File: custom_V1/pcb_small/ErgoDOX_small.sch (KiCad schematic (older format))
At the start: 61 parts, among them J1 Input, J10 Conn_01x01, J11 Conn_01x01, J12 Conn_01x01, J13 Conn_01x01, J14 Conn_01x01, J15 Conn_01x01, J16 Conn_01x01, J17 Conn_01x01, J18 Conn_01x01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

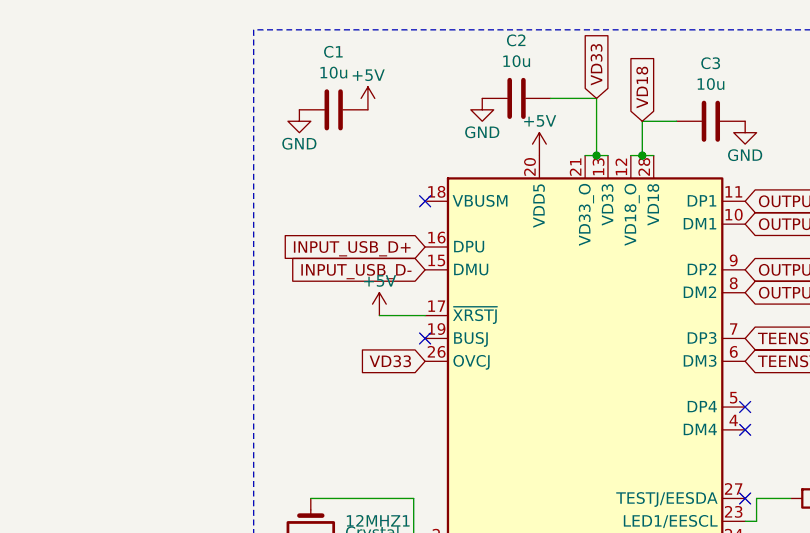
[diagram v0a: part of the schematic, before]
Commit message: add 1 mcu
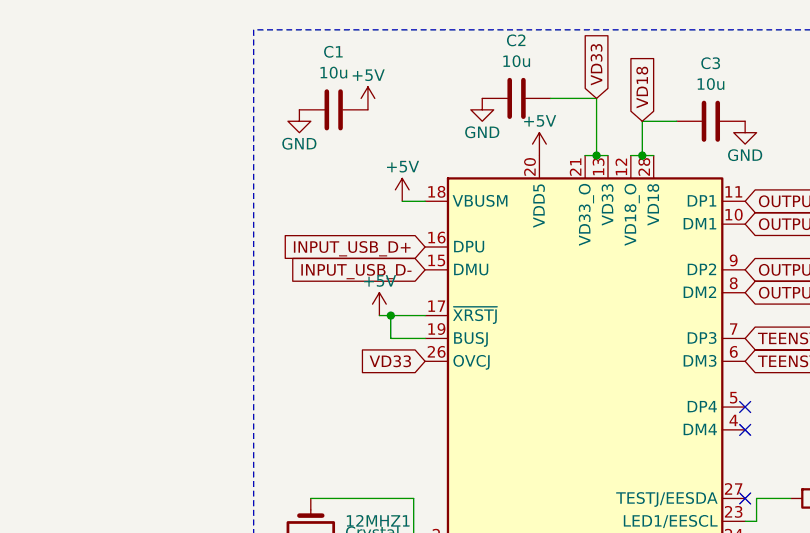
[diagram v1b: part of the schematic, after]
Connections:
- net +5V: now also U4.18 (VBUSM), U4.19 (BUSJ)
- no-connect marks 17 -> 15
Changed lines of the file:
@@
 EESchema Schematic File Version 4
-LIBS:ErgoDOX-cache
 EELAYER 26 0
 EELAYER END
@@
 NoConn ~ 11650 2250
 NoConn ~ 11650 2350
-NoConn ~ 10250 1350
-NoConn ~ 10250 1950
 $Comp
 L Device:C C1
@@
 $EndComp
 Wire Wire Line
-	10250 1850 10050 1850
+	10250 1850 10100 1850
 NoConn ~ 11650 2650
 $Comp
@@
 	1    0    0    -1
 $EndComp
+Wire Wire Line
+	10250 1950 10100 1950
+Wire Wire Line
+	10100 1950 10100 1850
+Connection ~ 10100 1850
+Wire Wire Line
+	10100 1850 10050 1850
+Wire Wire Line
+	10150 1350 10250 1350
+$Comp
+L power:+5V #PWR?
+U 1 1 60E773AA
+P 10150 1350
+F 0 "#PWR?" H 10150 1200 50  0001 C CNN
+F 1 "+5V" H 10150 1500 50  0000 C CNN
+F 2 "" H 10150 1350 50  0001 C CNN
+F 3 "" H 10150 1350 50  0001 C CNN
+	1    10150 1350
+	1    0    0    -1
+$EndComp
